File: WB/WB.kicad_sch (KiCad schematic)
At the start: 43 parts, among them J1 Conn_01x04, J2 Conn_01x04, J3 Conn_01x04, J4 Conn_01x04, J5 Pump, J6 Actuator, J7 Actuator, J8 Screw_Terminal_01x02, M1 Fan, Q1 Q_NMOS_GDS, Q2 Q_NMOS_GDS, Q3 Q_NMOS_GDS, Q4 Q_NMOS_GDS, Q5 Q_NMOS_GDS, Q6 Q_NMOS_GDS, Q7 Q_NMOS_GDS, Q8 Q_NPN_ECB, SW1 SW_Push, SW2 SW_Push, SW3 SW_Push, SW4 SW_Push, SW5 SW_Push, SW6 SW_Push, U1 74HC165, U2 74HC595, U3 TB6643KQ

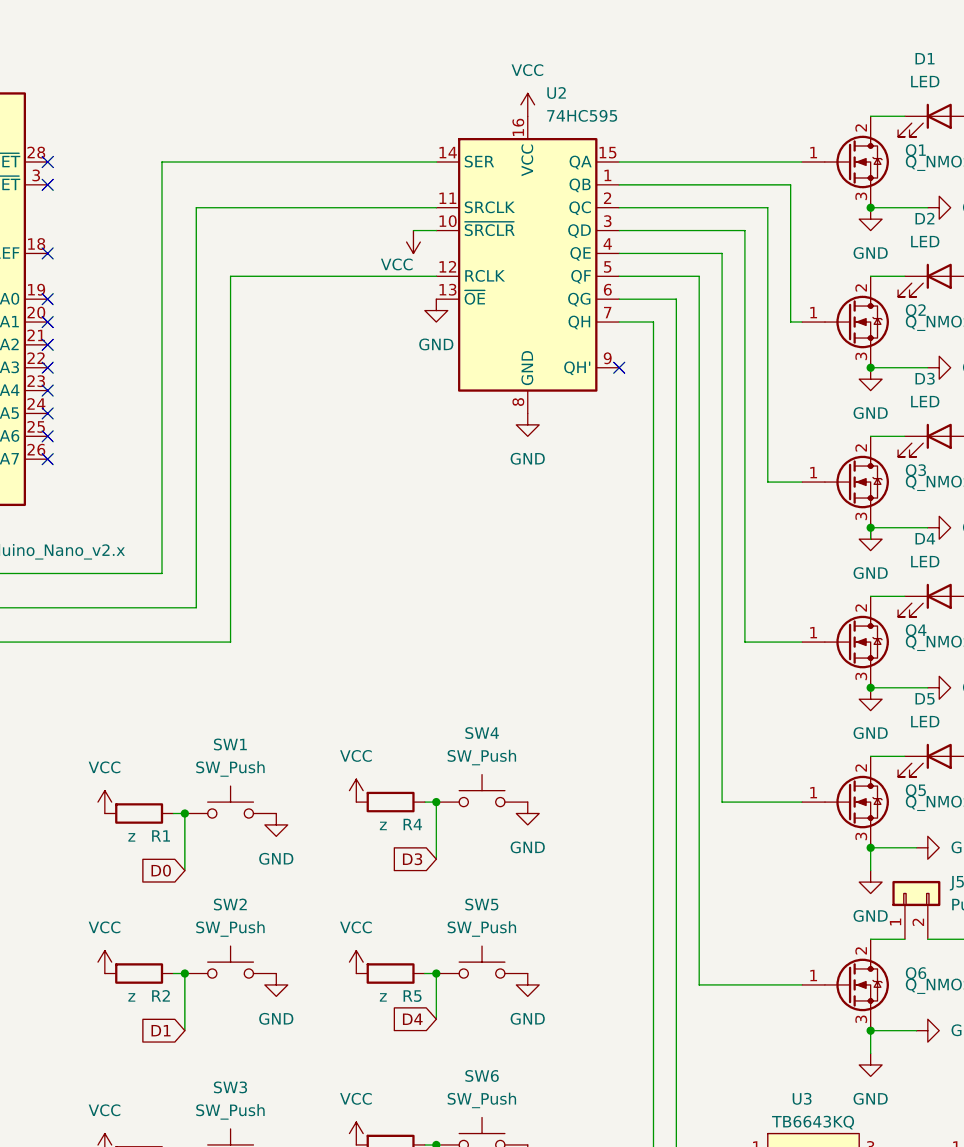
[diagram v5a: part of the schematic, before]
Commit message: 配線しやすいように回路を変更
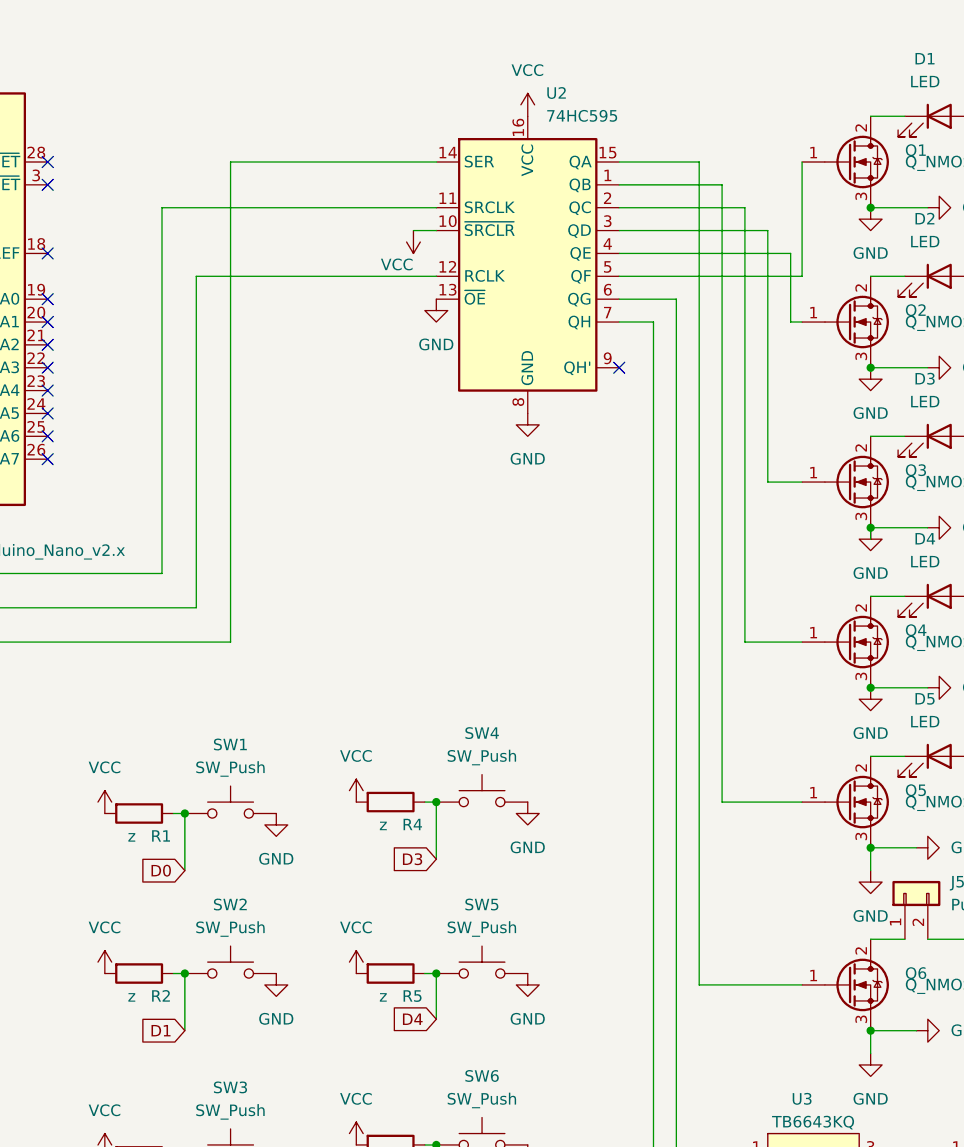
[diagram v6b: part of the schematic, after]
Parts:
- A1, A2, A3: footprint Module:Pololu_Breakout-16_15.2x20.3mm -> A4988_STEPPER_MOTOR_DRIVER_CARRIER:MODULE_A4988_STEPPER_MOTOR_DRIVER_CARRIER
- Q8: footprint Package_TO_SOT_THT:TO-92_Inline -> Package_TO_SOT_THT:TO-92L_Inline_Wide
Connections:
- net at Q1.1 (G): now also U2.5 (QF); no longer U2.15 (QA)
- net at Q5.1 (G): now also U2.1 (QB); no longer U2.4 (QE)
- net at A4.10 (D7): now also U2.12 (RCLK); no longer U2.11 (SRCLK)
- net at A4.11 (D8): now also U2.11 (SRCLK); no longer U2.14 (SER)
- net at A4.9 (D6): now also U2.14 (SER); no longer U2.12 (RCLK)
- net at Q3.1 (G): now also U2.3 (QD); no longer U2.2 (QC)
- net at Q2.1 (G): now also U2.4 (QE); no longer U2.1 (QB)
- net at Q4.1 (G): now also U2.2 (QC); no longer U2.3 (QD)
- net at Q6.1 (G): now also U2.15 (QA); no longer U2.5 (QF)
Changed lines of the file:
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@@
+    (stroke (width 0) (type default) (color 0 0 0 0))
+  )
+  (wire (pts (xy 200.66 41.91) (xy 173.99 41.91))
     (stroke (width 0) (type default) (color 0 0 0 0))
   )
@@
     (stroke (width 0) (type default) (color 0 0 0 0))
   )
+  (wire (pts (xy 241.3 29.21) (xy 241.3 41.91))
+    (stroke (width 0) (type default) (color 0 0 0 0))
+  )
   (wire (pts (xy 54.61 62.23) (xy 132.08 62.23))
     (stroke (width 0) (type default) (color 0 0 0 0))
   )
-  (wire (pts (xy 232.41 100.33) (xy 232.41 39.37))
+  (wire (pts (xy 232.41 31.75) (xy 232.41 100.33))
     (stroke (width 0) (type default) (color 0 0 0 0))
   )
@@
     (stroke (width 0) (type default) (color 0 0 0 0))
   )
+  (wire (pts (xy 232.41 31.75) (xy 220.98 31.75))
+    (stroke (width 0) (type default) (color 0 0 0 0))
+  )
   (wire (pts (xy 254 146.05) (xy 254 139.7))
     (stroke (width 0) (type default) (color 0 0 0 0))
@@
     (stroke (width 0) (type default) (color 0 0 0 0))
   )
-  (wire (pts (xy 220.98 34.29) (xy 237.49 34.29))
-    (stroke (width 0) (type default) (color 0 0 0 0))
-  )
   (wire (pts (xy 55.88 106.68) (xy 100.33 106.68))
     (stroke (width 0) (type default) (color 0 0 0 0))
@@
     (stroke (width 0) (type default) (color 0 0 0 0))
   )
+  (wire (pts (xy 229.87 29.21) (xy 220.98 29.21))
+    (stroke (width 0) (type default) (color 0 0 0 0))
+  )
   (wire (pts (xy 26.67 62.23) (xy 31.75 62.23))
     (stroke (width 0) (type default) (color 0 0 0 0))
@@
     (stroke (width 0) (type default) (color 0 0 0 0))
   )
-  (wire (pts (xy 220.98 31.75) (xy 240.03 31.75))
-    (stroke (width 0) (type default) (color 0 0 0 0))
-  )
   (wire (pts (xy 266.7 41.91) (xy 260.35 41.91))
     (stroke (width 0) (type default) (color 0 0 0 0))
@@
     (stroke (width 0) (type default) (color 0 0 0 0))
   )
-  (wire (pts (xy 200.66 34.29) (xy 173.99 34.29))
-    (stroke (width 0) (type default) (color 0 0 0 0))
-  )
-  (wire (pts (xy 234.95 36.83) (xy 234.95 82.55))
-    (stroke (width 0) (type default) (color 0 0 0 0))
-  )
-  (wire (pts (xy 220.98 36.83) (xy 234.95 36.83))
-    (stroke (width 0) (type default) (color 0 0 0 0))
-  )
-  (wire (pts (xy 220.98 29.21) (xy 241.3 29.21))
+  (wire (pts (xy 170.18 34.29) (xy 200.66 34.29))
+    (stroke (width 0) (type default) (color 0 0 0 0))
+  )
+  (wire (pts (xy 234.95 34.29) (xy 234.95 82.55))
     (stroke (width 0) (type default) (color 0 0 0 0))
   )
@@
     (stroke (width 0) (type default) (color 0 0 0 0))
   )
+  (wire (pts (xy 220.98 39.37) (xy 240.03 39.37))
+    (stroke (width 0) (type default) (color 0 0 0 0))
+  )
   (wire (pts (xy 251.46 142.24) (xy 256.54 142.24))
     (stroke (width 0) (type default) (color 0 0 0 0))
@@
     (stroke (width 0) (type default) (color 0 0 0 0))
   )
+  (wire (pts (xy 240.03 39.37) (xy 240.03 46.99))
+    (stroke (width 0) (type default) (color 0 0 0 0))
+  )
   (wire (pts (xy 266.7 77.47) (xy 260.35 77.47))
     (stroke (width 0) (type default) (color 0 0 0 0))
@@
     (stroke (width 0) (type default) (color 0 0 0 0))
   )
-  (wire (pts (xy 173.99 34.29) (xy 173.99 78.74))
-    (stroke (width 0) (type default) (color 0 0 0 0))
-  )
   (wire (pts (xy 234.95 82.55) (xy 241.3 82.55))
     (stroke (width 0) (type default) (color 0 0 0 0))
@@
     (stroke (width 0) (type default) (color 0 0 0 0))
   )
+  (wire (pts (xy 237.49 36.83) (xy 237.49 64.77))
+    (stroke (width 0) (type default) (color 0 0 0 0))
+  )
   (wire (pts (xy 139.7 129.54) (xy 146.05 129.54))
     (stroke (width 0) (type default) (color 0 0 0 0))
@@
     (stroke (width 0) (type default) (color 0 0 0 0))
   )
-  (wire (pts (xy 220.98 41.91) (xy 229.87 41.91))
-    (stroke (width 0) (type default) (color 0 0 0 0))
-  )
-  (wire (pts (xy 240.03 31.75) (xy 240.03 46.99))
-    (stroke (width 0) (type default) (color 0 0 0 0))
-  )
   (wire (pts (xy 27.94 59.69) (xy 31.75 59.69))
     (stroke (width 0) (type default) (color 0 0 0 0))
@@
     (stroke (width 0) (type default) (color 0 0 0 0))
   )
-  (wire (pts (xy 177.8 41.91) (xy 177.8 82.55))
+  (wire (pts (xy 177.8 29.21) (xy 177.8 82.55))
     (stroke (width 0) (type default) (color 0 0 0 0))
   )
@@
     (stroke (width 0) (type default) (color 0 0 0 0))
   )
+  (wire (pts (xy 241.3 41.91) (xy 220.98 41.91))
+    (stroke (width 0) (type default) (color 0 0 0 0))
+  )
   (wire (pts (xy 250.19 142.24) (xy 251.46 142.24))
     (stroke (width 0) (type default) (color 0 0 0 0))
@@
     (stroke (width 0) (type default) (color 0 0 0 0))
   )
+  (wire (pts (xy 237.49 36.83) (xy 220.98 36.83))
+    (stroke (width 0) (type default) (color 0 0 0 0))
+  )
   (wire (pts (xy 171.45 101.6) (xy 172.72 101.6))
     (stroke (width 0) (type default) (color 0 0 0 0))
@@
     (stroke (width 0) (type default) (color 0 0 0 0))
   )
-  (wire (pts (xy 200.66 41.91) (xy 177.8 41.91))
-    (stroke (width 0) (type default) (color 0 0 0 0))
-  )
-  (wire (pts (xy 229.87 41.91) (xy 229.87 120.65))
+  (wire (pts (xy 229.87 29.21) (xy 229.87 120.65))
     (stroke (width 0) (type default) (color 0 0 0 0))
   )
@@
     (stroke (width 0) (type default) (color 0 0 0 0))
   )
+  (wire (pts (xy 173.99 41.91) (xy 173.99 78.74))
+    (stroke (width 0) (type default) (color 0 0 0 0))
+  )
   (wire (pts (xy 199.39 100.33) (xy 200.66 100.33))
     (stroke (width 0) (type default) (color 0 0 0 0))
@@
     (stroke (width 0) (type default) (color 0 0 0 0))
   )
+  (wire (pts (xy 177.8 29.21) (xy 200.66 29.21))
+    (stroke (width 0) (type default) (color 0 0 0 0))
+  )
   (wire (pts (xy 26.67 160.02) (xy 33.02 160.02))
     (stroke (width 0) (type default) (color 0 0 0 0))
@@
     (stroke (width 0) (type default) (color 0 0 0 0))
   )
-  (wire (pts (xy 170.18 29.21) (xy 170.18 74.93))
+  (wire (pts (xy 170.18 34.29) (xy 170.18 74.93))
     (stroke (width 0) (type default) (color 0 0 0 0))
   )
@@
     (stroke (width 0) (type default) (color 0 0 0 0))
   )
+  (wire (pts (xy 234.95 34.29) (xy 220.98 34.29))
+    (stroke (width 0) (type default) (color 0 0 0 0))
+  )
   (wire (pts (xy 115.57 91.44) (xy 115.57 39.37))
     (stroke (width 0) (type default) (color 0 0 0 0))
@@
     (stroke (width 0) (type default) (color 0 0 0 0))
   )
-  (wire (pts (xy 237.49 34.29) (xy 237.49 64.77))
-    (stroke (width 0) (type default) (color 0 0 0 0))
-  )
   (wire (pts (xy 229.87 120.65) (xy 241.3 120.65))
     (stroke (width 0) (type default) (color 0 0 0 0))
@@
     (stroke (width 0) (type default) (color 0 0 0 0))
   )
-  (wire (pts (xy 170.18 29.21) (xy 200.66 29.21))
-    (stroke (width 0) (type default) (color 0 0 0 0))
-  )
   (wire (pts (xy 139.7 104.14) (xy 144.78 104.14))
     (stroke (width 0) (type default) (color 0 0 0 0))
@@
   )
   (wire (pts (xy 100.33 52.07) (xy 100.33 106.68))
-    (stroke (width 0) (type default) (color 0 0 0 0))
-  )
-  (wire (pts (xy 220.98 39.37) (xy 232.41 39.37))
     (stroke (width 0) (type default) (color 0 0 0 0))
   )
@@
       (effects (font (size 1.27 1.27)) (justify left))
     )
-    (property "Footprint" "Package_TO_SOT_THT:TO-92_Inline" (id 2) (at 78.74 154.94 0)
+    (property "Footprint" "Package_TO_SOT_THT:TO-92L_Inline_Wide" (id 2) (at 78.74 154.94 0)
       (effects (font (size 1.27 1.27)) hide)
     )
@@
       (effects (font (size 1.27 1.27)) (justify right))
     )
-    (property "Footprint" "Module:Pololu_Breakout-16_15.2x20.3mm" (id 2) (at 38.735 140.97 0)
+    (property "Footprint" "A4988_STEPPER_MOTOR_DRIVER_CARRIER:MODULE_A4988_STEPPER_MOTOR_DRIVER_CARRIER" (id 2) (at 38.735 140.97 0)
       (effects (font (size 1.27 1.27)) (justify left) hide)
     )
@@
       (effects (font (size 1.27 1.27)) (justify right))
     )
-    (property "Footprint" "Module:Pololu_Breakout-16_15.2x20.3mm" (id 2) (at 38.735 90.17 0)
+    (property "Footprint" "A4988_STEPPER_MOTOR_DRIVER_CARRIER:MODULE_A4988_STEPPER_MOTOR_DRIVER_CARRIER" (id 2) (at 38.735 90.17 0)
       (effects (font (size 1.27 1.27)) (justify left) hide)
     )
@@
       (effects (font (size 1.27 1.27)) (justify right))
     )
-    (property "Footprint" "Module:Pololu_Breakout-16_15.2x20.3mm" (id 2) (at 37.465 40.64 0)
+    (property "Footprint" "A4988_STEPPER_MOTOR_DRIVER_CARRIER:MODULE_A4988_STEPPER_MOTOR_DRIVER_CARRIER" (id 2) (at 37.465 40.64 0)
       (effects (font (size 1.27 1.27)) (justify left) hide)
     )
@@
     )
     (path "/e2dd1781-dd03-47fd-bd79-56dcdb6f3e26"
-      (reference "A1") (unit 1) (value "Pololu_Breakout_A4988") (footprint "Module:Pololu_Breakout-16_15.2x20.3mm")
+      (reference "A1") (unit 1) (value "Pololu_Breakout_A4988") (footprint "A4988_STEPPER_MOTOR_DRIVER_CARRIER:MODULE_A4988_STEPPER_MOTOR_DRIVER_CARRIER")
     )
     (path "/37037ec8-1abd-4989-95cb-9d98e310cd33"
-      (reference "A2") (unit 1) (value "Pololu_Breakout_A4988") (footprint "Module:Pololu_Breakout-16_15.2x20.3mm")
+      (reference "A2") (unit 1) (value "Pololu_Breakout_A4988") (footprint "A4988_STEPPER_MOTOR_DRIVER_CARRIER:MODULE_A4988_STEPPER_MOTOR_DRIVER_CARRIER")
     )
     (path "/06c52993-5f84-43fc-a946-b617228fa9ca"
-      (reference "A3") (unit 1) (value "Pololu_Breakout_A4988") (footprint "Module:Pololu_Breakout-16_15.2x20.3mm")
+      (reference "A3") (unit 1) (value "Pololu_Breakout_A4988") (footprint "A4988_STEPPER_MOTOR_DRIVER_CARRIER:MODULE_A4988_STEPPER_MOTOR_DRIVER_CARRIER")
     )
     (path "/3f18b2c4-1cdc-4686-8bef-57f6b4b93a54"
@@
     )
     (path "/04990d8a-7035-45bc-bf9d-2eacd4b35133"
-      (reference "Q8") (unit 1) (value "Q_NPN_ECB") (footprint "Package_TO_SOT_THT:TO-92_Inline")
+      (reference "Q8") (unit 1) (value "Q_NPN_ECB") (footprint "Package_TO_SOT_THT:TO-92L_Inline_Wide")
     )
     (path "/1999e1ca-2fa7-4a51-a19c-76f8cd528547"

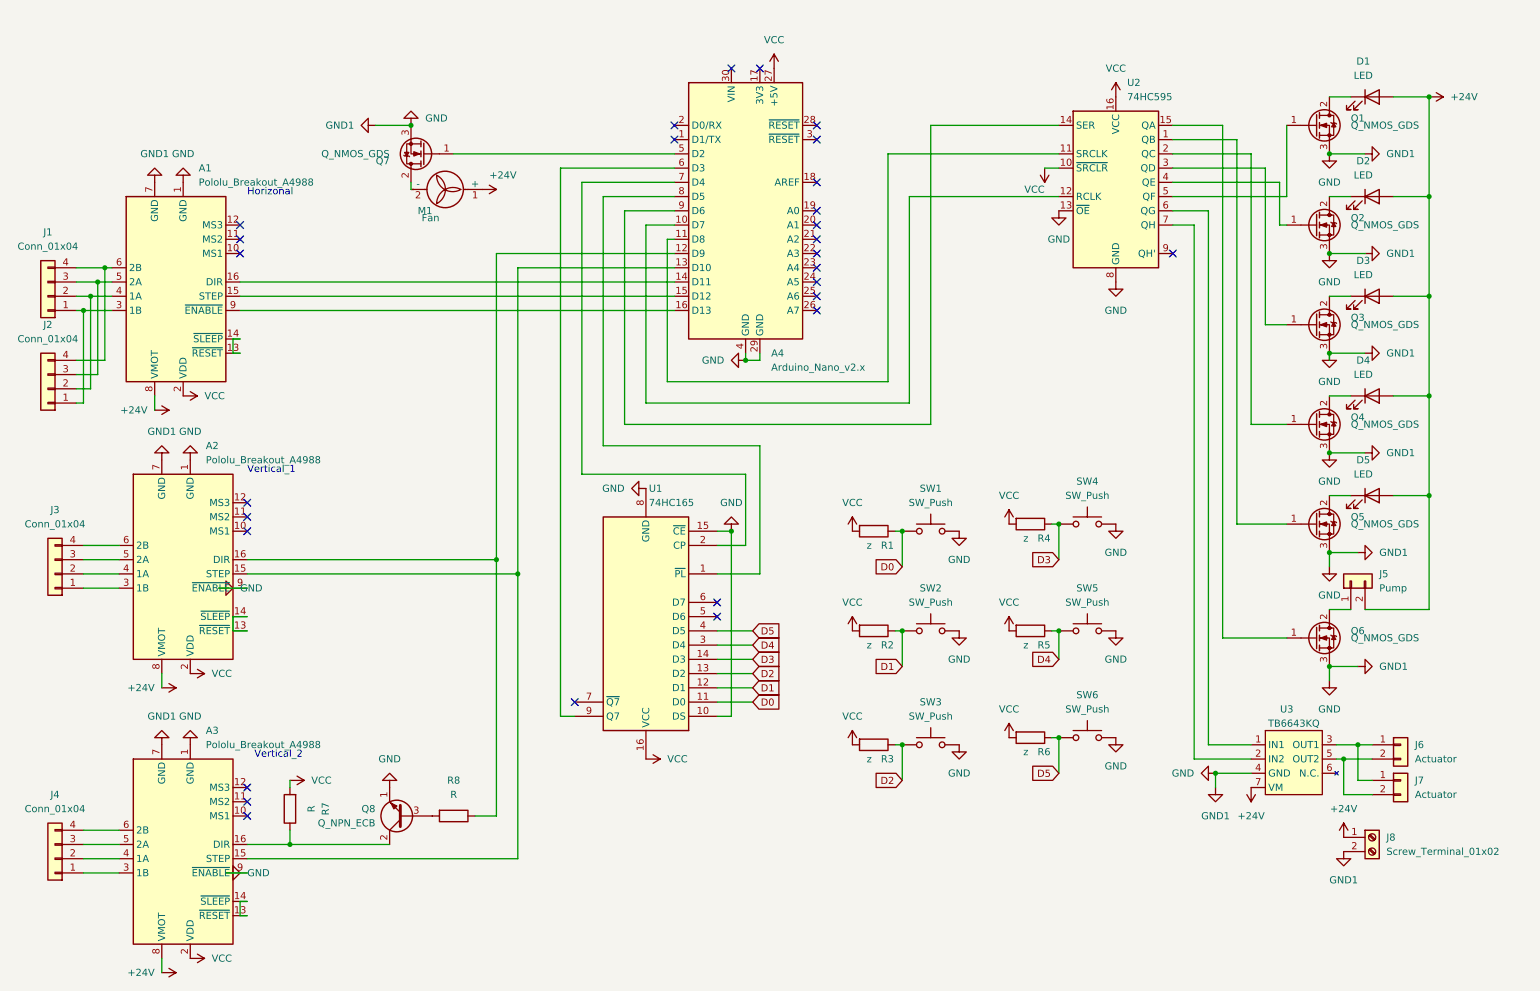
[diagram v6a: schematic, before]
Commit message: メインマイコンの変更
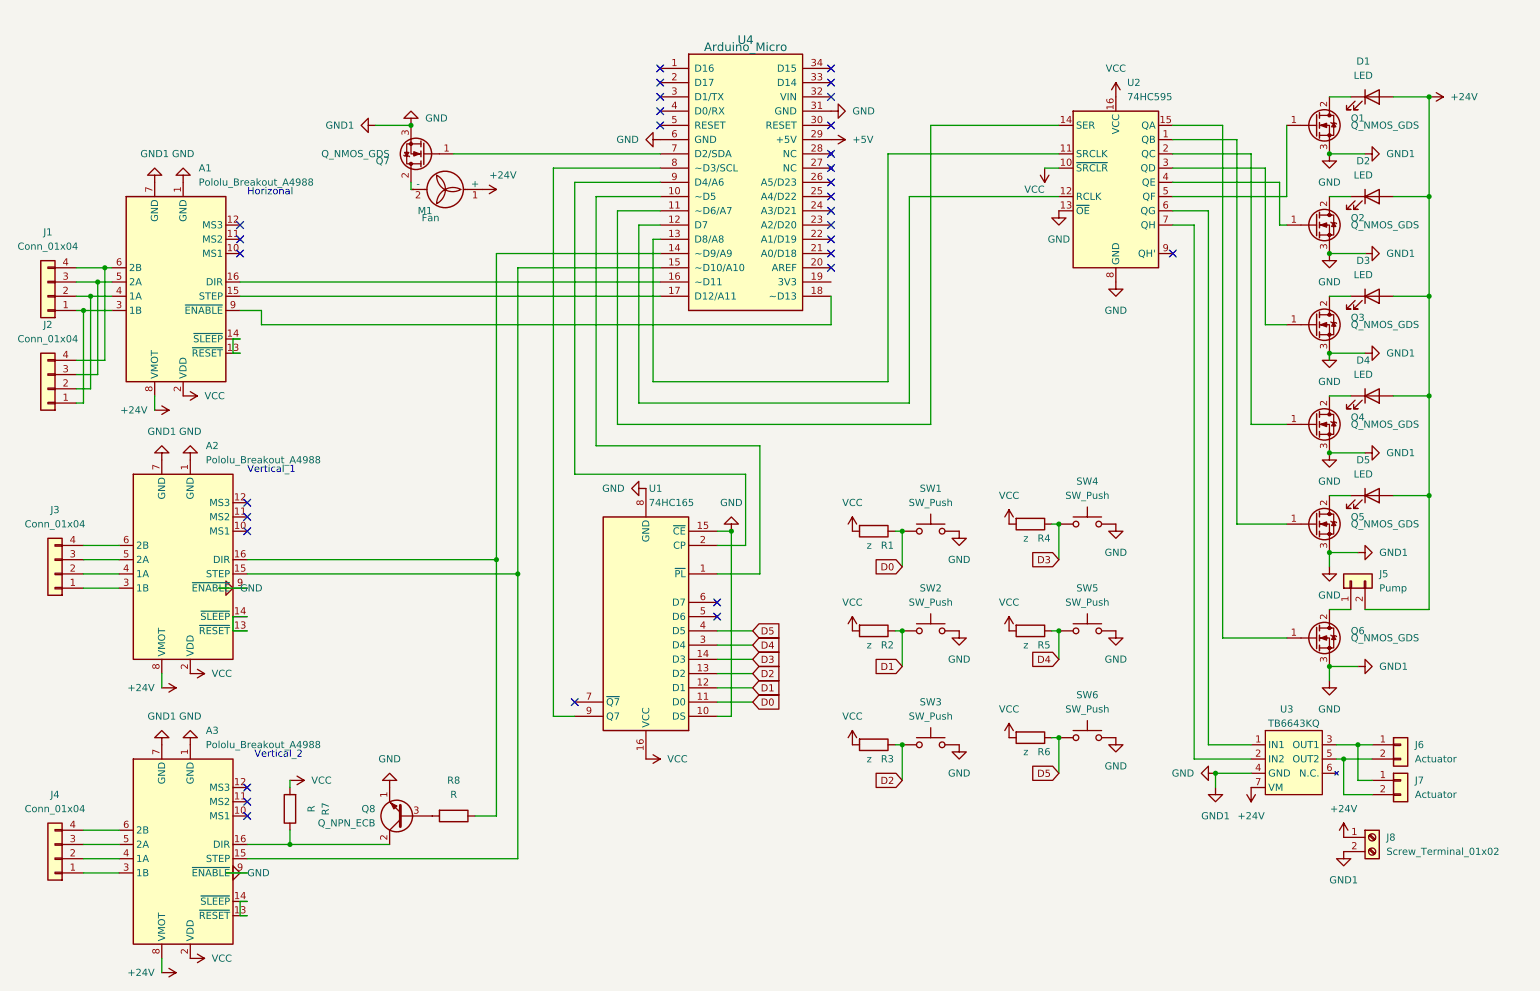
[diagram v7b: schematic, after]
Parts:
- removed A4: Arduino_Nano_v2.x, Module:Arduino_Nano, symbol MCU_Module:Arduino_Nano_v2.x
- added U4: Arduino_Micro, Arduino:Arduino_Micro, symbol Arduino:Arduino_Micro
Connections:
- net GND: now also U4.31 (GND), U4.6 (GND)
- net at A2.15 (STEP), A3.15 (STEP): now also U4.15 (~D10/A10)
- net at A2.16 (DIR), R8.1: now also U4.14 (~D9/A9)
- net at U2.12 (RCLK): now also U4.12 (D7)
- net at U2.11 (SRCLK): now also U4.13 (D8/A8)
- net at A1.16 (DIR): now also U4.16 (~D11)
- net at A1.15 (STEP): now also U4.17 (D12/A11)
- net at A1.9 (~{ENABLE}): now also U4.18 (~D13)
- net at Q7.1 (G): now also U4.7 (D2/SDA)
- net at U1.9 (Q7): now also U4.8 (~D3/SCL)
- net at U1.2 (CP): now also U4.9 (D4/A6)
- net at U1.1 (~{PL}): now also U4.10 (~D5)
- net at U2.14 (SER): now also U4.11 (~D6/A7)
- new net +5V: U4.29 (+5V)
- no-connect marks 28 -> 31

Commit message: 回路図の修正
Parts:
- added C1, C3, C4: C, Capacitor_THT:C_Rect_L4.0mm_W2.5mm_P2.50mm, symbol Device:C
- added C2: C, Capacitor_THT:C_Radial_D8.0mm_H11.5mm_P3.50mm, symbol Device:C
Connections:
- net +24V: now also C1.2, C2.2
- net GND: now also C1.1, C2.1
- net at J6.1 (Pin_1), J7.1 (Pin_1), U3.3 (OUT1): now also C3.1, C4.1
- net at J6.2 (Pin_2), J7.2 (Pin_2), U3.5 (OUT2): now also C3.2, C4.2
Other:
- moved on the sheet: J6, J7, J8
